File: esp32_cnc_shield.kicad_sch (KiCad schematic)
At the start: 18 parts

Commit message: PCB
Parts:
- removed J?: Configuration, Connector_PinHeader_2.54mm:PinHeader_2x06_P2.54mm_Vertical, symbol Connector_Generic:Conn_02x06_Counter_Clockwise
- removed J?: UART, Connector_PinHeader_1.27mm:PinHeader_1x02_P1.27mm_Vertical, symbol Connector_Generic:Conn_01x02
- removed J?: USB_B_Micro, Connector_USB:USB_Micro-AB_Molex_47590-0001, symbol Connector:USB_B_Micro
- added J1: USB C, usbc:USB_C_Cursed, symbol Connector:Barrel_Jack_MountingPin
- added J2: UART, Connector_PinHeader_2.54mm:PinHeader_1x03_P2.54mm_Vertical, symbol Connector_Generic:Conn_01x03
- added J7: Configuration, Connector_PinHeader_2.54mm:PinHeader_1x03_P2.54mm_Vertical, symbol Connector_Generic:Conn_02x05_Counter_Clockwise
- added JP1: Future Shotky, symbol Jumper:Jumper_2_Open
- gave numbers to parts that had none: 15
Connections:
- net +3.3V: now also JP1.2 (B)
- net DIR_X: now also U1.30 (GPIO18_VSPI-CLK); no longer U1.29 (GPIO5_VSPI-CS0)
- net DIR_Z: now also U1.25 (GPIO2_ADC2-CH2_RTC-GPIO12); no longer U1.30 (GPIO18_VSPI-CLK)
- net GND: now also J1.2, J1.MP (MountPin), J2.3 (Pin_3), J7.10 (Pin_10), J7.6 (Pin_6), J7.7 (Pin_7), J7.8 (Pin_8), J7.9 (Pin_9)
- net STEP_X: now also U1.29 (GPIO5_VSPI-CS0); no longer U1.26 (GPIO4_ADC2-CH0_RTC-GPIO10)
- net STEP_Y: now also U1.28 (GPIO17_UART2-TX); no longer U1.13 (GPIO13_ADC2-CH4_HSPI-MOSI_RTC-GPIO14)
- net STEP_Z: now also U1.26 (GPIO4_ADC2-CH0_RTC-GPIO10), J7.4 (Pin_4); no longer U1.28 (GPIO17_UART2-TX)
- net STOP_X: now also U1.36 (GPIO23_VSPI-MOSI), J7.1 (Pin_1); no longer U1.10 (GPIO27_ADC2-CH7_RTC-GPIO17)
- net STOP_Y: now also U1.35 (GPIO22_I2C-SCL), J7.2 (Pin_2); no longer U1.6 (GPIO32_ADC1-CH4_RTC-GPIO9)
- net STOP_Z: now also U1.32 (GPIO21_I2C-SDA), J7.3 (Pin_3); no longer U1.7 (GPIO33_ADC1-CH5_RTC-GPIO8)
- net VCC: now also J1.1, J7.5 (Pin_5), JP1.1 (A)
- net rx: now also J2.2 (Pin_2)
- net tx: now also J2.1 (Pin_1)
- no-connect marks 4 -> 26
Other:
- company: Grzegorz Kupczyk /Hagis -> (none)
- moved on the sheet: U1

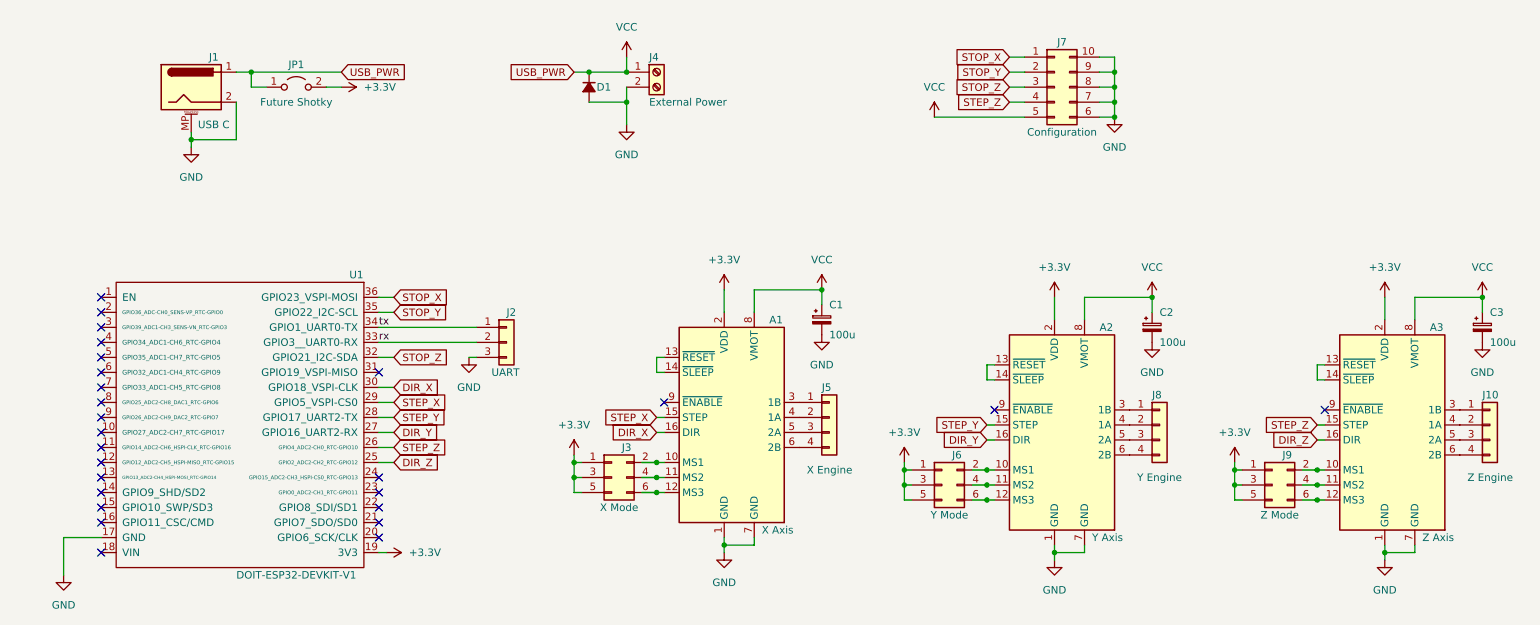
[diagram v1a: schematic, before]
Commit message: Add pseudo shottky
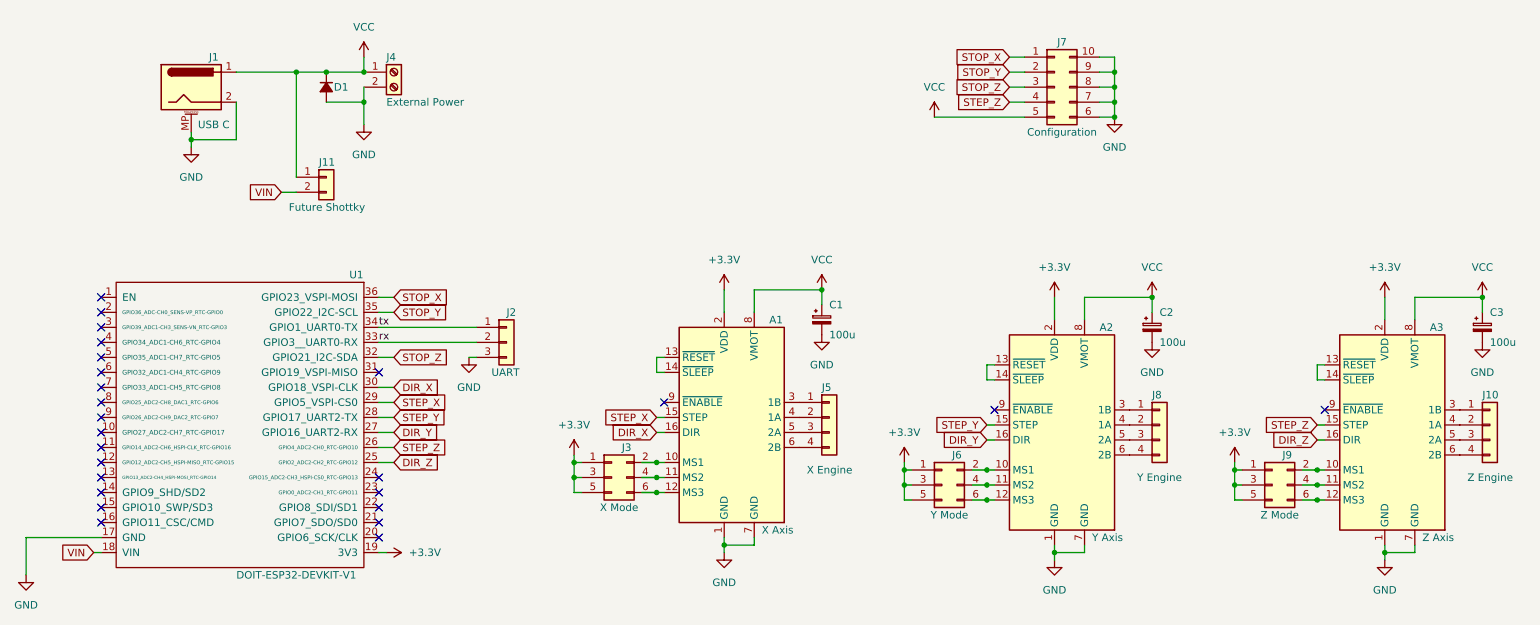
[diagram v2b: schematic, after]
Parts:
- removed JP1: Future Shotky, symbol Jumper:Jumper_2_Open
- added J11: Future Shottky, symbol Connector_Generic:Conn_01x02
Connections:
- net VCC: now also J11.1 (Pin_1)
- net VIN: now reaches U1.18 (VIN)
- net VIN: now also J11.2 (Pin_2)
- no-connect marks 26 -> 25
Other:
- moved on the sheet: D1, J4
